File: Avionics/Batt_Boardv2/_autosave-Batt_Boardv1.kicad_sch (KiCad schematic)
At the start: 43 parts, among them J3 Screw_Terminal_01x01, J4 JST_PH_S2B-PH-SM4, J5 Screw_Terminal_01x02, J6 Screw_Terminal_01x02, J7 Screw_Terminal_01x02, J8 Screw_Terminal_01x02, Q1 IRF7458, Q2 IRF7458, U3 TMP36xS

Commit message: just need traces
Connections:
- net Pack -: now also H1.1, H2.1, H3.1, H4.1
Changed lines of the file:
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@@
+	)
+	(junction
+		(at 232.41 81.28)
+		(diameter 0)
+		(color 0 0 0 0)
 	)
 	(junction
@@
 		)
 		(stroke
+			(width 0)
+			(type default)
+		)
+	)
+	(wire
+		(pts
+			(xy 232.41 59.69) (xy 232.41 81.28)
+		)
+		(stroke

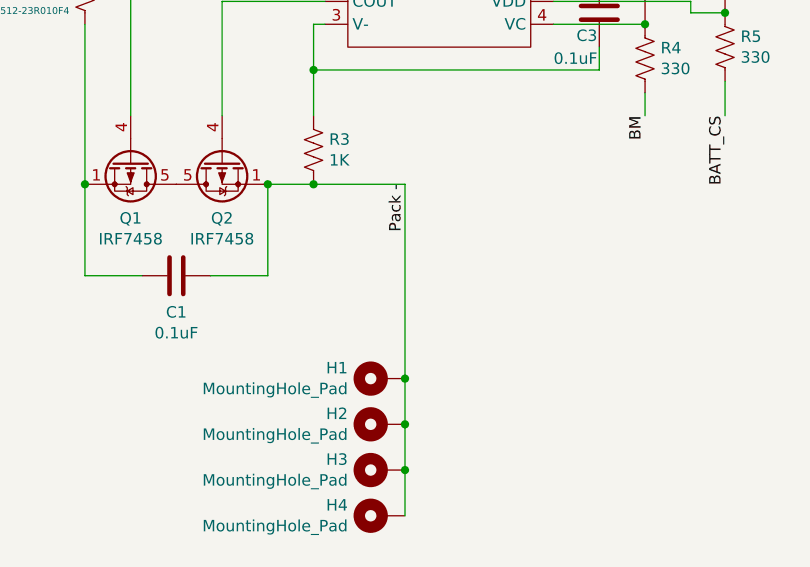
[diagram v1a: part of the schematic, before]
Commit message: 12/3/2024, Sephora Poteau: changed PC104 layout to include copper layer and edge cuts, and changed placement of components on Batt_Boardv2
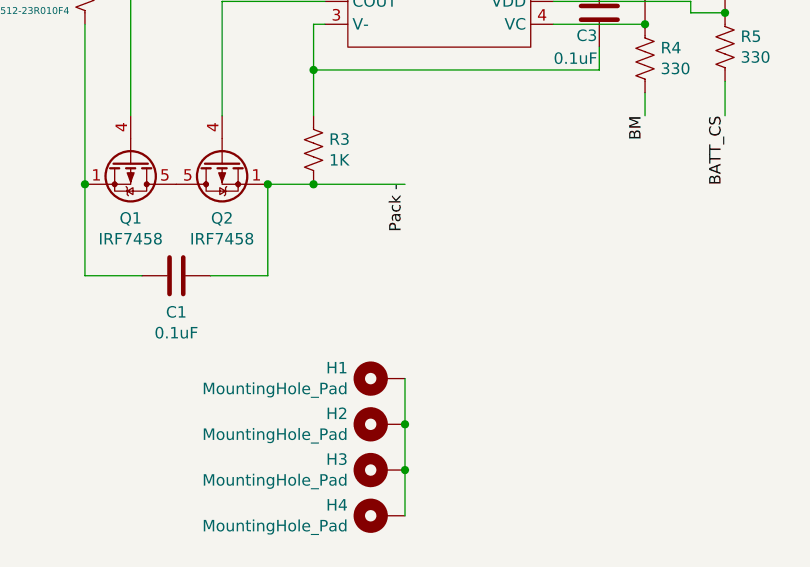
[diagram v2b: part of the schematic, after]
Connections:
- net Pack -: no longer H1.1, H2.1, H3.1, H4.1
- new net: H1.1, H2.1, H3.1, H4.1
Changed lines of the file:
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@@
-	)
-	(junction
-		(at 232.41 81.28)
-		(diameter 0)
-		(color 0 0 0 0)
 	)
 	(junction
@@
 		)
 		(stroke
-			(width 0)
-			(type default)
-		)
-	)
-	(wire
-		(pts
-			(xy 232.41 59.69) (xy 232.41 81.28)
-		)
-		(stroke
